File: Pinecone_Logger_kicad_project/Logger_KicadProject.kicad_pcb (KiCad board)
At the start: 4 copper layers, 63.5 x 52.3 mm, 50 parts, among them J1 PJ-102A, J2 M50-3600542, J3 DM3AT-SF-PEJM5, J4 OSTVN06A150, J5 OSTVN06A150, J6 OSTVN06A150, J7 OSTVN06A150, J8 10_Pin_Header, Q1 AO3420, Q2 AO3420, Q3 AO3420, Q4 AO3420, U1 SAMD20E16A-A, U2 MIC5211, U3 AP2281, U4 DS1302, U5 MAX4618, U6 MAX31856, Y1 MC-306_32.768K-E3

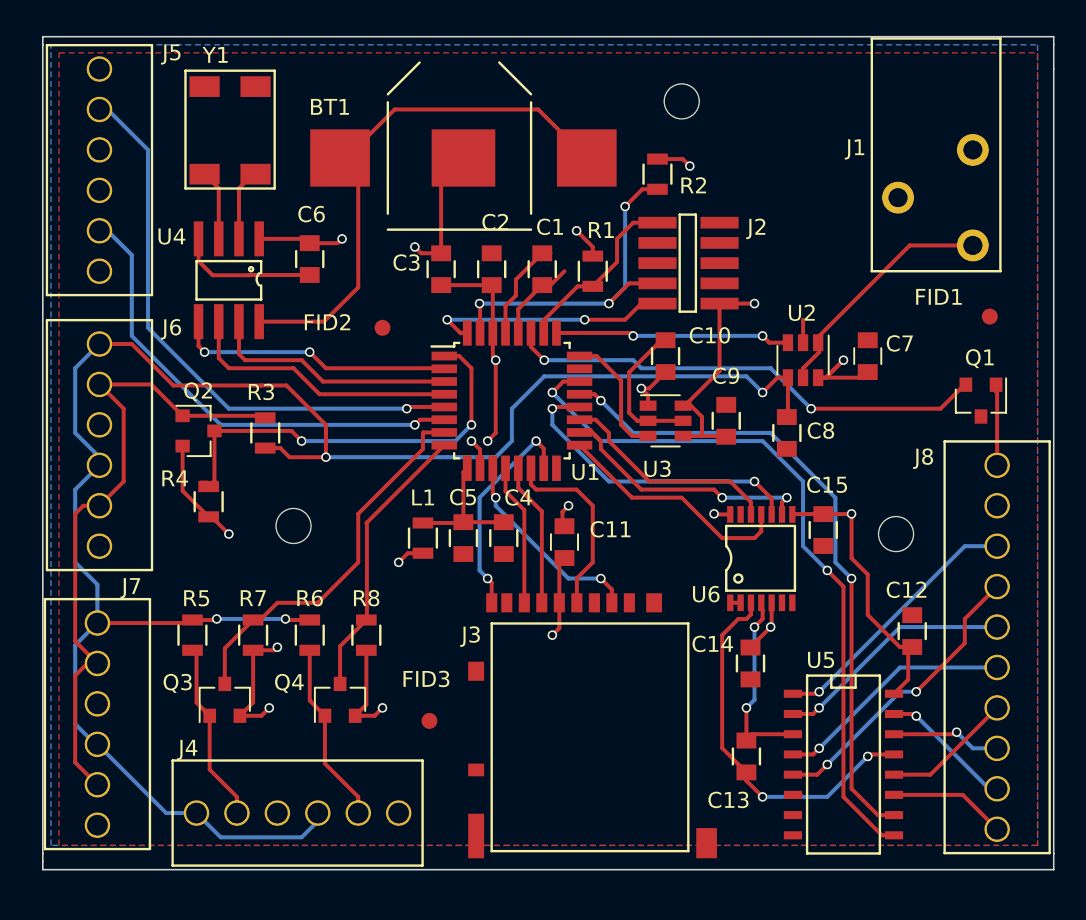
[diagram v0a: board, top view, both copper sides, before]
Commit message: bunch of minor changes, changed DS1302 crystal to through hole with correst ESD
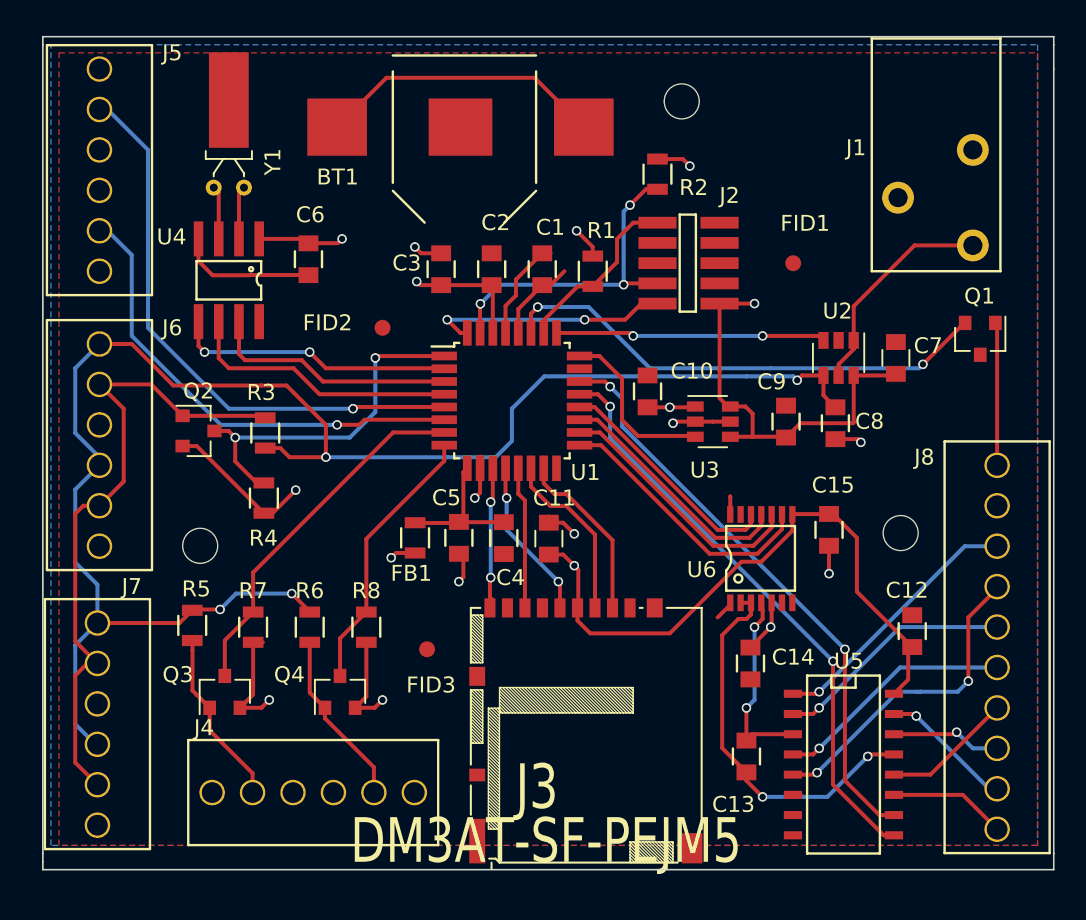
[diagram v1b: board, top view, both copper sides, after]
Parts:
- J3: footprint Pinecone_footprints:Hirose_DM3AT -> Pinecone_logger_footprints:hirose-dm3at
- Y1: value MC-306_32.768K-E3 -> CFS-20632768EZBB; footprint Pinecone_footprints:MC-306_32.768K-E3 -> Crystals:Crystal_DS26_d2.0mm_l6.0mm_Horizontal_1EP_style1
- moved BT1 15.4 mm to (47.7, 38.7), turned to 180 degrees
- moved FID1 12.8 mm to (60.9, 47.2)
- moved J3 8.74 mm to (50.6, 69.5)
- moved REF** 5.99 mm to (23.6, 65.0)
- moved FID3 4.50 mm to (37.9, 71.5)
- moved Q1 3.88 mm to (72.6, 52.0)
- moved C9 3.76 mm to (60.4, 57.2)
- moved R4 3.48 mm to (27.6, 62.0)
- moved C8 3.11 mm to (63.5, 57.3)
- moved U3 2.97 mm to (55.8, 57.2)
- moved Y1 2.61 mm to (26.4, 42.5), turned to 180 degrees
- moved C10 2.49 mm to (51.7, 55.3)
- moved U2 2.24 mm to (63.7, 53.2)
- moved C7 1.77 mm to (67.3, 53.2)
- moved J4 1.62 mm to (24.4, 80.5)
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- renumbered L1 to FB1
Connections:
- J3 pad 10: (no net) -> Net-(J3-Pad10)
- J3 pad 9: (no net) -> Net-(J3-Pad9)
- U1 pad 11: SD_SERCOM_PAD0_MISO -> SD_CHIP_DETECT
- U1 pad 12: SD_SERCOM_PAD1_CS -> SD_SERCOM_PAD3_SCK
- U1 pad 13: SD_SERCOM_PAD2_MOSI -> SD_SERCOM_PAD0_MISO
- U1 pad 14: SD_SERCOM_PAD3_SCK -> SD_SERCOM_PAD2_MOSI
- U1 pad 15: SD_CHIP_DETECT -> SD_SERCOM_PAD1_CS
- U1 pad 17: MAX31856_SERCOM_PAD0_MISO -> MAX31856_SERCOM_PAD1_CS
- U1 pad 18: MAX31856_SERCOM_PAD1_CS -> MAX31856_SERCOM_PAD3_SCK
- U1 pad 19: MAX31856_SERCOM_PAD2_MOSI -> MAX31856_SERCOM_PAD0_MISO
- U1 pad 20: MAX31856_SERCOM_PAD3_SCK -> MAX31856_SERCOM_PAD2_MOSI
- U1 pad 21: MUX_SEL_A -> MUX_SEL_B
- U1 pad 22: MUX_SEL_B -> MUX_SEL_A
- U6 pad 2: GND -> Net-(C13-Pad2)
- Y1 pad 1: Net-(U4-Pad3) -> Net-(U4-Pad2)
- Y1 pad 2: Net-(Y1-Pad2) -> Net-(U4-Pad3)
- Y1 pad 3: Net-(Y1-Pad3) -> (no net)
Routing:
- net SWITCHED_3v3: track 50.1 -> 68.7 mm, vias 8 -> 6
- net Net-(BT1-Pad1): track 34.3 -> 18.1 mm
- net MUX_SEL_B: track 45.1 -> 36.9 mm
- net GND: track 39.3 -> 34.0 mm, vias 4 -> 7
- net SD_CHIP_DETECT: track 14.1 -> 9.10 mm
- net SDI_3v3_DATA: track 26.5 -> 22.6 mm
- net HEATER_SWITCHED_GND: track 5.20 -> 9.02 mm
- net SD_SERCOM_PAD0_MISO: track 12.7 -> 8.94 mm, vias 2 -> 0
- net MUX_SEL_A: track 40.8 -> 37.4 mm
- net MAX31856_SERCOM_PAD3_SCK: track 19.5 -> 16.4 mm, vias 2 -> 0
- net SWITCHED_5v: track 118.2 -> 121.2 mm
- net 3v3_PWR_ENABLE: track 8.02 -> 10.9 mm
- net 5v_PWR_ENABLE: track 14.8 -> 17.0 mm
- net SD_SERCOM_PAD1_CS: track 8.94 -> 11.0 mm
- net SD_SERCOM_PAD2_MOSI: track 9.06 -> 11.0 mm
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- added copper zone on Vcc.Cu, net SWITCHED_5v
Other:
- rule trace_min: 0.2 -> 0.25
- board text removed: "Design by Tim Anderson Univ. Montana"

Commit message: completed revision of circuit design, remapped pins in conf_board
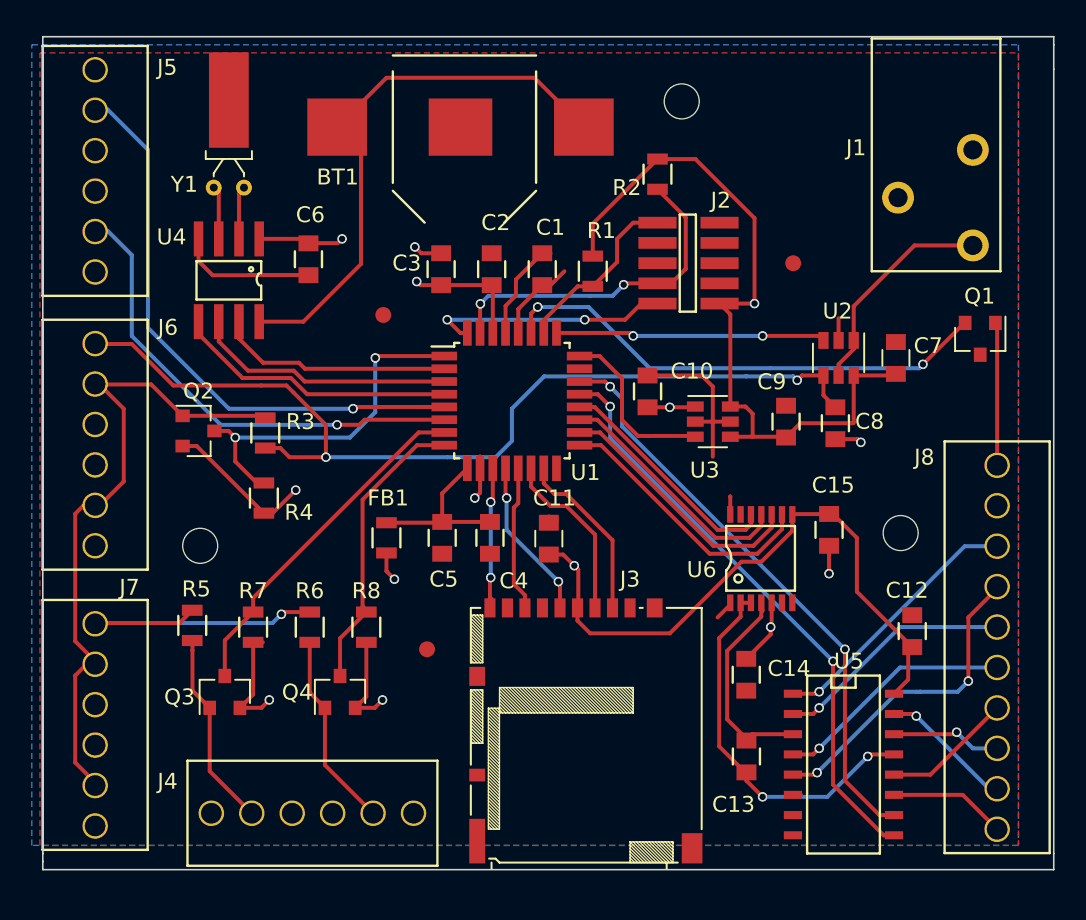
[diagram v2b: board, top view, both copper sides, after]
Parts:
- moved FB1 1.80 mm to (35.3, 64.5)
- moved J4 1.30 mm to (24.3, 81.8)
- moved C5 1.05 mm to (38.8, 64.5)
- moved C4 0.87 mm to (41.8, 64.5)
- moved FID2 0.81 mm to (35.1, 50.5)
- moved C14 0.76 mm to (57.9, 73.1)
- moved J5 0.28 mm to (17.0, 35.1)
- moved J6 0.27 mm to (17.0, 52.3)
- moved J7 0.15 mm to (17.0, 69.9)
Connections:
- U1 pad 2: DS1302_CE -> DS1302_SCLK
- U1 pad 3: DS1302_SCLK -> DS1302_IO
- U1 pad 4: DS1302_IO -> DS1302_CE
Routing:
- net SWITCHED_5v: track 121.2 -> 80.5 mm, vias 4 -> 3
- net +3V3: track 45.3 -> 62.6 mm, vias 6 -> 4
- net Net-(BT1-Pad1): track 18.1 -> 35.2 mm
- net GND: track 34.0 -> 39.1 mm, vias 7 -> 4
- net Net-(C4-Pad2): track 8.59 -> 10.7 mm
- net Net-(C13-Pad1): track 12.2 -> 13.6 mm, vias 2 -> 0
- net Net-(J4-Pad5): track 11.1 -> 12.4 mm
- net Net-(J4-Pad2): track 11.6 -> 12.9 mm
- net DHT22_2: track 17.3 -> 18.5 mm
- net DS1302_IO: track 17.4 -> 16.5 mm
- net DHT22_1: track 23.4 -> 22.5 mm
- net DS1302_SCLK: track 15.6 -> 14.8 mm
- net SWITCHED_3v3: track 68.7 -> 69.4 mm
- net SWDCLK: track 20.8 -> 21.4 mm, vias 3 -> 2
- net DS1302_CE: track 17.6 -> 17.8 mm, vias 2 -> 0

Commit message: changed SOT-23 MOSFETS to have correct pinout. design should work with AO3420's now
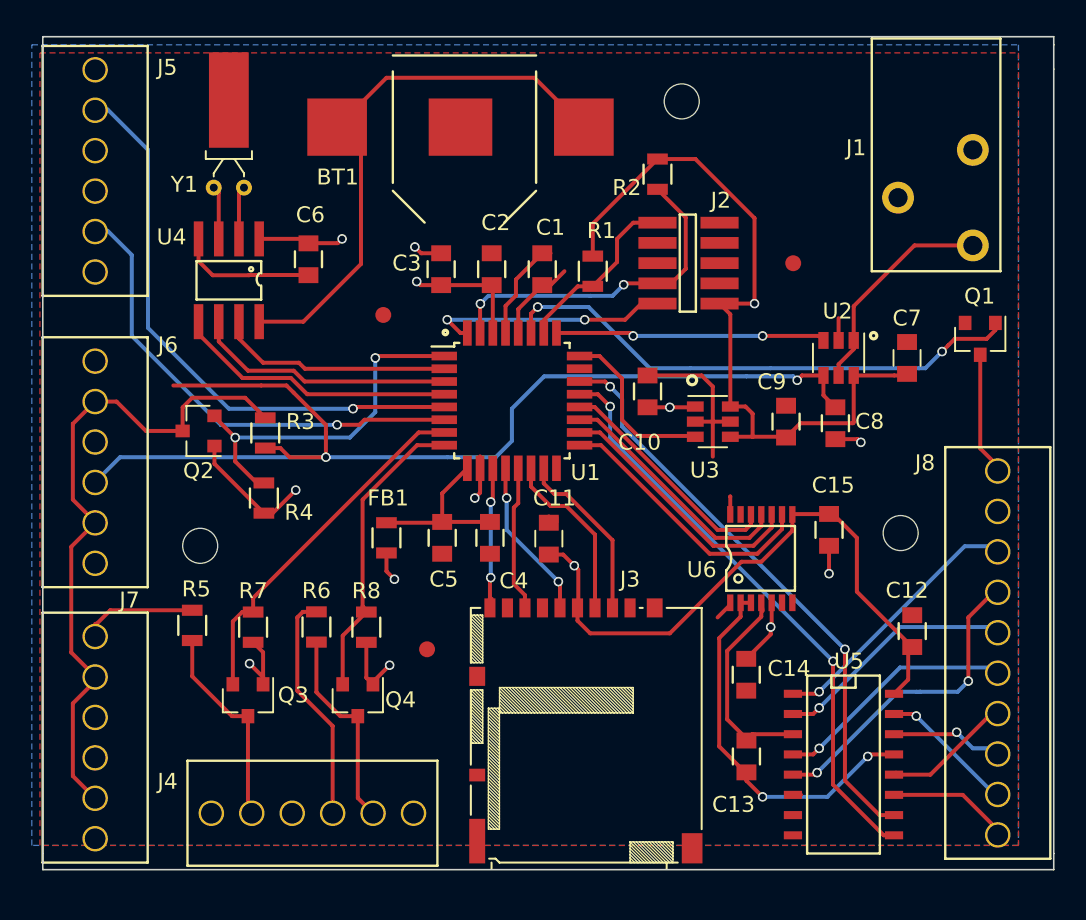
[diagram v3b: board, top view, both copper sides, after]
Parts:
- moved Q3 1.55 mm to (26.6, 74.7), turned to 270 degrees
- moved Q4 1.23 mm to (33.5, 74.7), turned to 270 degrees
- moved J6 1.10 mm to (17.0, 53.4)
- moved J7 0.80 mm to (17.0, 70.7)
- moved C7 0.70 mm to (68.0, 53.2)
- moved R6 0.42 mm to (30.9, 70.1)
- moved J8 0.36 mm to (73.7, 60.3)
- turned Q2 to 180 degrees
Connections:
- Q1 pad 1: HEATER_SWITCHED_GND -> HEATER_ENABLE
- Q1 pad 2: HEATER_ENABLE -> GND
- Q1 pad 3: GND -> HEATER_SWITCHED_GND
- Q2 pad 1: Net-(J6-Pad2) -> SWITCHED_3v3
- Q2 pad 2: SWITCHED_3v3 -> SDI_3v3_DATA
- Q2 pad 3: SDI_3v3_DATA -> Net-(J6-Pad2)
- Q3 pad 1: Net-(J4-Pad2) -> SWITCHED_3v3
- Q3 pad 2: SWITCHED_3v3 -> DHT22_1
- Q3 pad 3: DHT22_1 -> Net-(J4-Pad2)
- Q4 pad 1: Net-(J4-Pad5) -> SWITCHED_3v3
- Q4 pad 2: SWITCHED_3v3 -> DHT22_2
- Q4 pad 3: DHT22_2 -> Net-(J4-Pad5)
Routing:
- net SWITCHED_5v: track 80.5 -> 90.0 mm, vias 3 -> 2
- net SWITCHED_3v3: track 69.4 -> 64.2 mm
- net HEATER_ENABLE: track 31.4 -> 33.6 mm
- net HEATER_SWITCHED_GND: track 9.02 -> 7.38 mm
- net Net-(J6-Pad2): track 40.6 -> 42.2 mm
- net DHT22_1: track 22.5 -> 23.2 mm
- net +3V3: track 62.6 -> 63.3 mm

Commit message: updated power jack footprint
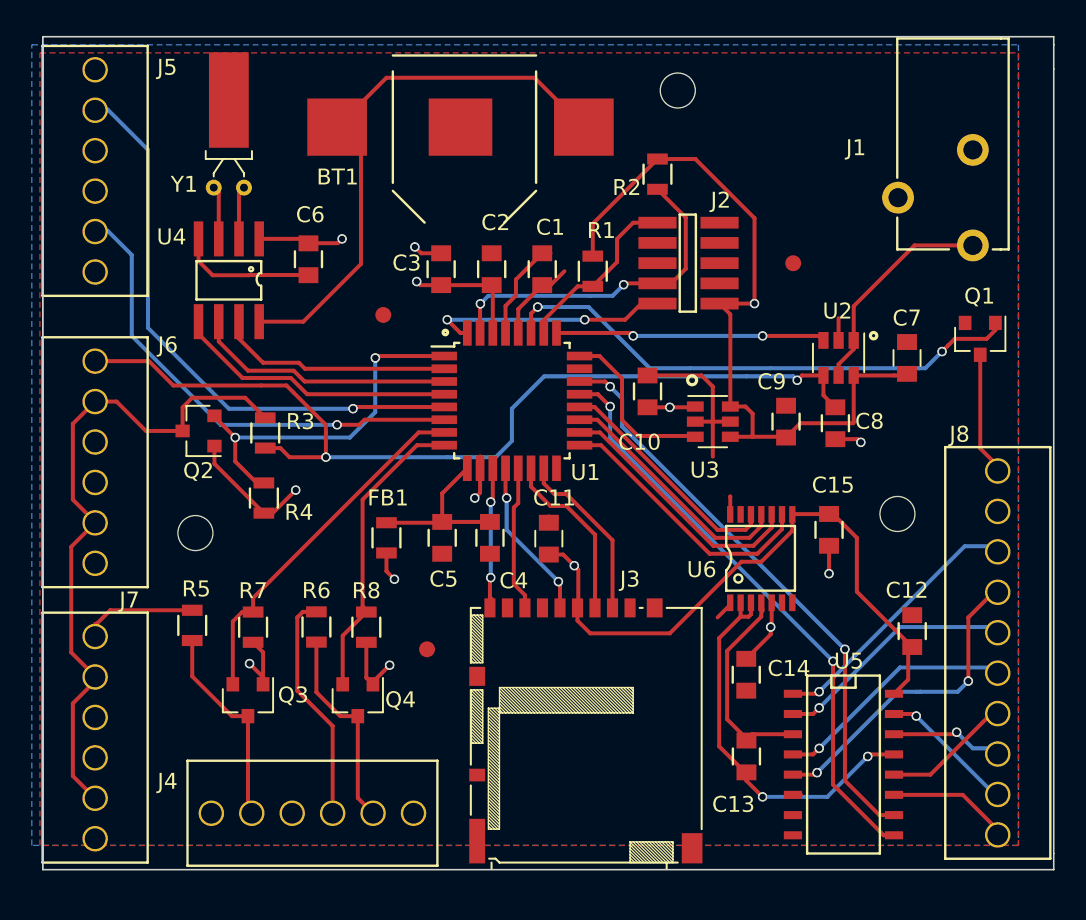
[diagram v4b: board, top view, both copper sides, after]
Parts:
- J1: footprint Pinecone_footprints:PJ-102A -> Pinecone_logger_footprints:PJ-102A
- moved REF** 1.22 mm to (67.4, 63.0)
- moved REF** 0.85 mm to (23.3, 64.2)
- moved REF** 0.73 mm to (53.6, 36.4)
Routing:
- net SWITCHED_5v: track 90.0 -> 80.4 mm
- net Net-(C13-Pad2): track 23.9 -> 24.7 mm
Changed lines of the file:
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@@
     (thickness 1.6)
     (drawings 27)
-    (tracks 489)
+    (tracks 491)
     (zones 0)
     (modules 50)
@@
     )
   )
-  (module Pinecone_footprints:PJ-102A (layer F.Cu)
-    (at 72.136 40.132)
-    (fp_text reference J1 (at -7.336 -0.132) (layer F.SilkS)
-      (effects (font (size 1 1) (thickness 0.15)))
-    )
-    (fp_text value PJ-102A (at -3.81 -8.89) (layer F.Fab)
-      (effects (font (size 1 1) (thickness 0.15)))
-    )
-    (fp_line (start 1.73 -7) (end 1.73 7.62) (layer F.SilkS) (width 0.15))
-    (fp_line (start 1.73 7.62) (end -6.35 7.62) (layer F.SilkS) (width 0.15))
-    (fp_line (start -6.35 7.62) (end -6.35 -7) (layer F.SilkS) (width 0.15))
-    (fp_line (start -6.35 -7) (end 1.73 -7) (layer F.SilkS) (width 0.15))
-    (pad 1 thru_hole circle (at 0 6) (size 2 2) (drill 1.2) (layers *.Cu *.Mask)
-      (net 8 +12V))
-    (pad 3 thru_hole circle (at -4.7 3) (size 2 2) (drill 1.2) (layers *.Cu *.Mask)
-      (net 9 "Net-(J1-Pad3)"))
-    (pad 2 thru_hole circle (at 0 0) (size 2 2) (drill 1.2) (layers *.Cu *.Mask)
-      (net 2 GND))
-  )
   (module Pinecone_footprints:10_Pin_Cortex_SMD (layer F.Cu)
     (at 52.324 49.784 90)
@@
   (module Pinecone_footprints:OSTVN10A150_10_pin_term (layer F.Cu)
     (at 73.7 60.3 270)
-    (fp_text reference J8 (at -0.508 4.572 360) (layer F.SilkS)
+    (fp_text reference J8 (at -2.3 2.4 360) (layer F.SilkS)
       (effects (font (size 1 1) (thickness 0.15)))
     )
@@
   )
   (module Mounting_Holes:MountingHole_2.2mm_M2 (layer F.Cu)
-    (at 67.6 64.2)
+    (at 67.4 63)
     (descr "Mounting Hole 2.2mm, no annular, M2")
     (tags "mounting hole 2.2mm no annular m2")
@@
   )
   (module Mounting_Holes:MountingHole_2.2mm_M2 (layer F.Cu)
-    (at 23.6 65)
+    (at 23.3 64.2)
     (descr "Mounting Hole 2.2mm, no annular, M2")
     (tags "mounting hole 2.2mm no annular m2")
@@
   )
   (module Mounting_Holes:MountingHole_2.2mm_M2 (layer F.Cu)
-    (at 53.848 37.084)
+    (at 53.6 36.4)
     (descr "Mounting Hole 2.2mm, no annular, M2")
     (tags "mounting hole 2.2mm no annular m2")
@@
       (solder_mask_margin 0.127) (clearance 0.254))
   )
+  (module Pinecone_logger_footprints:PJ-102A (layer F.Cu)
+    (at 72.136 40.132)
+    (fp_text reference J1 (at -7.336 -0.132) (layer F.SilkS)
+      (effects (font (size 1 1) (thickness 0.15)))
+    )
+    (fp_text value PJ-102A (at -3.81 -8.89) (layer F.Fab)
+      (effects (font (size 1 1) (thickness 0.15)))
+    )
+    (fp_line (start 2.25 -7) (end 1.75 -7) (layer F.SilkS) (width 0.15))
+    (fp_line (start 1.75 6.25) (end 2.25 6.25) (layer F.SilkS) (width 0.15))
+    (fp_line (start 1.25 6.25) (end 1.75 6.25) (layer F.SilkS) (width 0.15))
+    (fp_line (start 2.25 6.25) (end 2.25 -7) (layer F.SilkS) (width 0.15))
+    (fp_line (start -4.75 4.25) (end -4.75 6.25) (layer F.SilkS) (width 0.15))
+    (fp_line (start -4.75 6.25) (end -1.5 6.25) (layer F.SilkS) (width 0.15))
+    (fp_line (start 1.75 -7) (end -4.75 -7) (layer F.SilkS) (width 0.15))
+    (fp_line (start -4.75 1.75) (end -4.75 -7) (layer F.SilkS) (width 0.15))
+    (pad 1 thru_hole circle (at 0 6) (size 2 2) (drill 1.2) (layers *.Cu *.Mask)
+      (net 8 +12V))
+    (pad 3 thru_hole circle (at -4.7 3) (size 2 2) (drill 1.2) (layers *.Cu *.Mask)
+      (net 9 "Net-(J1-Pad3)"))
+    (pad 2 thru_hole circle (at 0 0) (size 2 2) (drill 1.2) (layers *.Cu *.Mask)
+      (net 2 GND))
+  )
   (gr_circle (center 65.9 51.8) (end 65.9 52) (layer F.SilkS) (width 0.2))
   (gr_circle (center 54.5 54.6) (end 54.7 54.8) (layer F.SilkS) (width 0.2))
@@
   (segment (start 60.818 63.008) (end 60.796 63.03) (width 0.25) (layer F.Cu) (net 6))
   (segment (start 60.818 63.008) (end 60.796 63.03) (width 0.25) (layer F.Cu) (net 6))
+  (segment (start 17 53.4) (end 20.38 53.4) (width 0.25) (layer F.Cu) (net 7))
+  (segment (start 29.022 54.93) (end 27.432 54.93) (width 0.25) (layer F.Cu) (net 7))
+  (segment (start 31.496 57.404) (end 29.464 55.372) (width 0.25) (layer F.Cu) (net 7))
+  (segment (start 31.496 57.912) (end 31.496 57.404) (width 0.25) (layer F.Cu) (net 7))
+  (segment (start 31.496 57.912) (end 31.496 59.436) (width 0.25) (layer F.Cu) (net 7))
+  (segment (start 27.432 54.93) (end 21.91 54.93) (width 0.25) (layer F.Cu) (net 7))
+  (segment (start 29.022 54.93) (end 29.464 55.372) (width 0.25) (layer F.Cu) (net 7))
+  (segment (start 20.38 53.4) (end 21.91 54.93) (width 0.25) (layer F.Cu) (net 7))
   (segment (start 17 61.02) (end 17 61) (width 0.25) (layer B.Cu) (net 7))
-  (segment (start 17 61) (end 18.564 59.436) (width 0.25) (layer B.Cu) (net 7))
-  (segment (start 18.564 59.436) (end 31.496 59.436) (width 0.25) (layer B.Cu) (net 7))
   (segment (start 30.9 69.15) (end 30.05 69.15) (width 0.25) (layer F.Cu) (net 7))
   (segment (start 31.92 76.32) (end 31.92 81.8) (width 0.25) (layer F.Cu) (net 7))
@@
   (segment (start 62.75 54.3) (end 62.75 55.55) (width 0.25) (layer F.Cu) (net 7))
   (segment (start 62.75 55.55) (end 63.5 56.3) (width 0.25) (layer F.Cu) (net 7))
-  (segment (start 29.022 54.93) (end 29.464 55.372) (width 0.25) (layer F.Cu) (net 7))
-  (segment (start 27.432 54.93) (end 21.91 54.93) (width 0.25) (layer F.Cu) (net 7))
-  (segment (start 31.496 59.436) (end 31.496 57.912) (width 0.25) (layer F.Cu) (net 7))
-  (segment (start 31.496 57.912) (end 31.496 57.404) (width 0.25) (layer F.Cu) (net 7))
-  (segment (start 31.496 57.404) (end 29.464 55.372) (width 0.25) (layer F.Cu) (net 7))
-  (segment (start 29.022 54.93) (end 27.432 54.93) (width 0.25) (layer F.Cu) (net 7))
   (segment (start 30.48 69.13) (end 30.48 69.162) (width 0.25) (layer F.Cu) (net 7))
   (segment (start 27.686 58.862) (end 28.636 58.862) (width 0.25) (layer F.Cu) (net 7))
@@
   (segment (start 58.277 76.835) (end 57.912 77.2) (width 0.25) (layer F.Cu) (net 60))
   (segment (start 58.928 69.088) (end 58.846 68.58) (width 0.25) (layer F.Cu) (net 60))
+  (segment (start 57.546 69.454) (end 58.046 69.454) (width 0.25) (layer F.Cu) (net 61))
+  (segment (start 58.196 69.304) (end 58.196 68.58) (width 0.25) (layer F.Cu) (net 61))
+  (segment (start 58.046 69.454) (end 58.196 69.304) (width 0.25) (layer F.Cu) (net 61))
   (segment (start 57.912 79.232) (end 57.832 79.232) (width 0.25) (layer F.Cu) (net 61))
   (segment (start 57.832 79.232) (end 56.2 77.6) (width 0.25) (layer F.Cu) (net 61))
@@
   (via (at 58.928 80.772) (size 0.6) (drill 0.4) (layers F.Cu B.Cu) (net 61))
   (segment (start 58.928 80.772) (end 57.912 79.756) (width 0.25) (layer F.Cu) (net 61))
-  (segment (start 57.546 68.58) (end 58.196 68.58) (width 0.25) (layer F.Cu) (net 61))
   (segment (start 57.912 79.756) (end 57.912 79.232) (width 0.25) (layer F.Cu) (net 61))
   (zone (net 4) (net_name +3V3) (layer Vcc.Cu) (hatch edge 0.508)
